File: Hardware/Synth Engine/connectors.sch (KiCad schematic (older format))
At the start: 8 parts, among them J10 Conn_01x13, J11 Conn_01x13, J8 Conn_01x13, J9 Conn_01x13

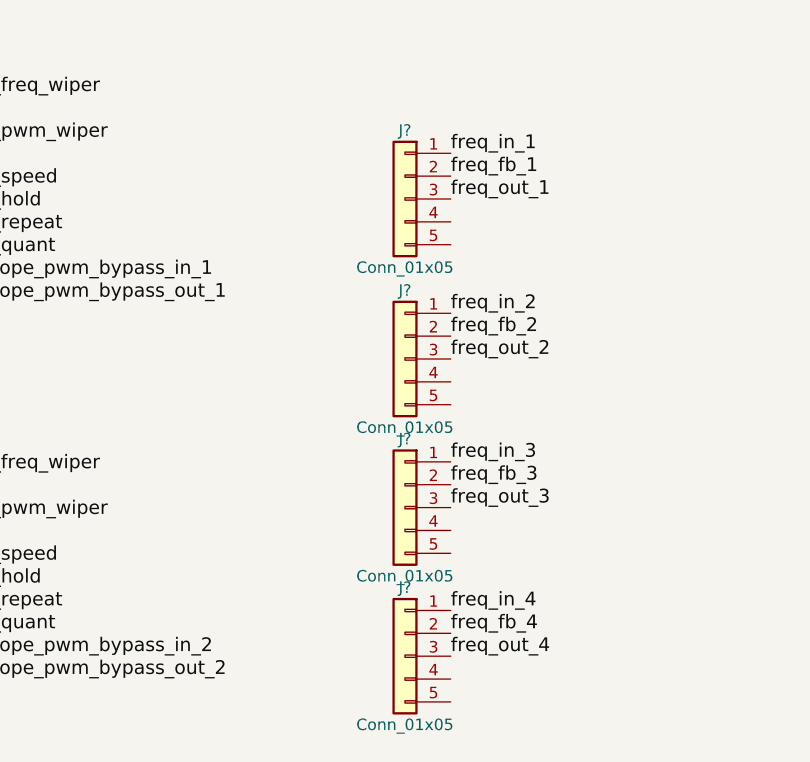
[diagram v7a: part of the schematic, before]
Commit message: correct placement of filter connectors, and they are placed relative to the ADC connectors. This should result in mating connection between both boards.
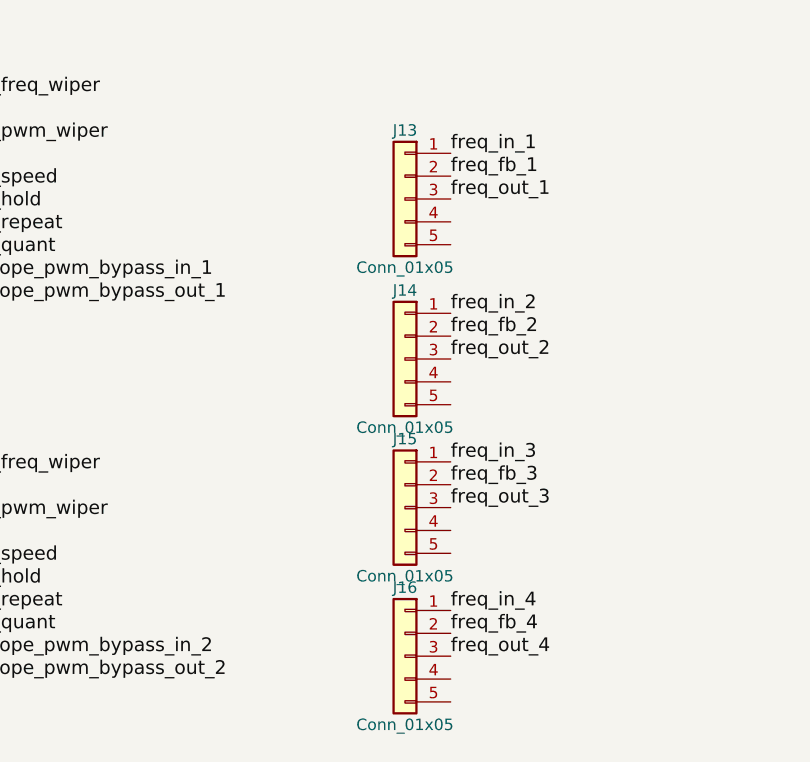
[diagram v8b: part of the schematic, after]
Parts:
- J13, J14, J15, J16: renamed from J?; footprint (none) -> Pin_Headers:Pin_Header_Straight_1x05_Pitch2.54mm
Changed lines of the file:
@@
 $EndComp
 $Comp
-L Conn_01x05 J?
+L Conn_01x05 J13
 U 1 1 5C639754
 P 3600 1350
-F 0 "J?" H 3600 1650 50  0000 C CNN
+F 0 "J13" H 3600 1650 50  0000 C CNN
 F 1 "Conn_01x05" H 3600 1050 50  0000 C CNN
-F 2 "" H 3600 1350 50  0001 C CNN
+F 2 "Pin_Headers:Pin_Header_Straight_1x05_Pitch2.54mm" H 3600 1350 50  0001 C CNN
 F 3 "" H 3600 1350 50  0001 C CNN
 	1    3600 1350
@@
 $EndComp
 $Comp
-L Conn_01x05 J?
+L Conn_01x05 J14
 U 1 1 5C6397E0
 P 3600 2050
-F 0 "J?" H 3600 2350 50  0000 C CNN
+F 0 "J14" H 3600 2350 50  0000 C CNN
 F 1 "Conn_01x05" H 3600 1750 50  0000 C CNN
-F 2 "" H 3600 2050 50  0001 C CNN
+F 2 "Pin_Headers:Pin_Header_Straight_1x05_Pitch2.54mm" H 3600 2050 50  0001 C CNN
 F 3 "" H 3600 2050 50  0001 C CNN
 	1    3600 2050
@@
 $EndComp
 $Comp
-L Conn_01x05 J?
+L Conn_01x05 J15
 U 1 1 5C63986E
 P 3600 2700
-F 0 "J?" H 3600 3000 50  0000 C CNN
+F 0 "J15" H 3600 3000 50  0000 C CNN
 F 1 "Conn_01x05" H 3600 2400 50  0000 C CNN
-F 2 "" H 3600 2700 50  0001 C CNN
+F 2 "Pin_Headers:Pin_Header_Straight_1x05_Pitch2.54mm" H 3600 2700 50  0001 C CNN
 F 3 "" H 3600 2700 50  0001 C CNN
 	1    3600 2700
@@
 $EndComp
 $Comp
-L Conn_01x05 J?
+L Conn_01x05 J16
 U 1 1 5C6398B4
 P 3600 3350
-F 0 "J?" H 3600 3650 50  0000 C CNN
+F 0 "J16" H 3600 3650 50  0000 C CNN
 F 1 "Conn_01x05" H 3600 3050 50  0000 C CNN
-F 2 "" H 3600 3350 50  0001 C CNN
+F 2 "Pin_Headers:Pin_Header_Straight_1x05_Pitch2.54mm" H 3600 3350 50  0001 C CNN
 F 3 "" H 3600 3350 50  0001 C CNN
 	1    3600 3350
